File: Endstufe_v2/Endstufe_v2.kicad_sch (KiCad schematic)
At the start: 0 parts

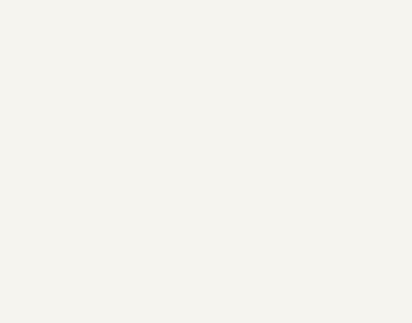
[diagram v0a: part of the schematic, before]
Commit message: Add SigmaStudio trial project and libraries for ADAU1701 and S/PDIF connector
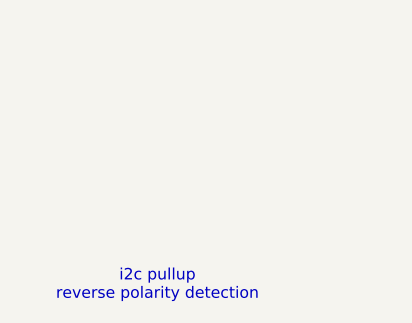
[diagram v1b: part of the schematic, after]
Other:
- note added: "i2c pullup reverse polarity detection"
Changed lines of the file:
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@@
 	(generator_version "8.0")
 	(paper "A4")
+	(text "i2c pullup\nreverse polarity detection"
+		(exclude_from_sim no)
+		(at 49.276 127.254 0)
+		(effects
+			(font
+				(size 1.27 1.27)
+			)
+		)
+	)
 	(sheet
 		(at 46.99 43.18)
